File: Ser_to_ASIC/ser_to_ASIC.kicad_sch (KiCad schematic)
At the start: 44 parts, among them J1 MOLEX-524653071, J2 CONMHF4-SMD-G-T, J4 MOLEX-524653071, U1 ADP160AUJZ-1.2-R7, U2 ADP121-AUJZ12R7, U3 10M02DCV36I7G, U4 DS90UB913ATRTVJQ1, U5 TC2015-1.8VCTTR, U6 LT1761ES5-3.3-TRPBF, X1 EG-2102CA 100.0000M-PHPAL3

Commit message: Update ser_to_ASIC.kicad_sch
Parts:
- added C18: 10uF, symbol Device:C
- added R1, R10, R11: 10k, Resistor_SMD:R_0201_0603Metric, symbol Device:R_US
- added R2: 100k, Resistor_SMD:R_0201_0603Metric, symbol Device:R_US
- added SW1: R-668049, jonnew:MITSUMI_R-668049, symbol Switch:SW_Push
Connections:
- net +1V8: now also R1.2
- net +3.3V: now also R10.1, R11.1
- net G: now also U4.7 (RES), C18.2, R10.2, R2.1, SW1.1
- net SCL_SER: no longer R8.1, U4.4 (SCL)
- net SDA_SER: no longer R7.1, U4.5 (SDA)
- net at U4.8 (MODE): now also R1.1, R2.2
- net at U4.9 (PDB): now also C18.1, R11.2, SW1.2
- net ID_X: no longer names the net of R5.1, R6.1, U4.6 (ID[X])
- new net: R8.1, U4.4 (SCL)
- new net: R7.1, U4.5 (SDA)
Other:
- moved on the sheet: C1, C11, C12, C15, C16, C17, C2, C20, C21, C22, C23, C24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

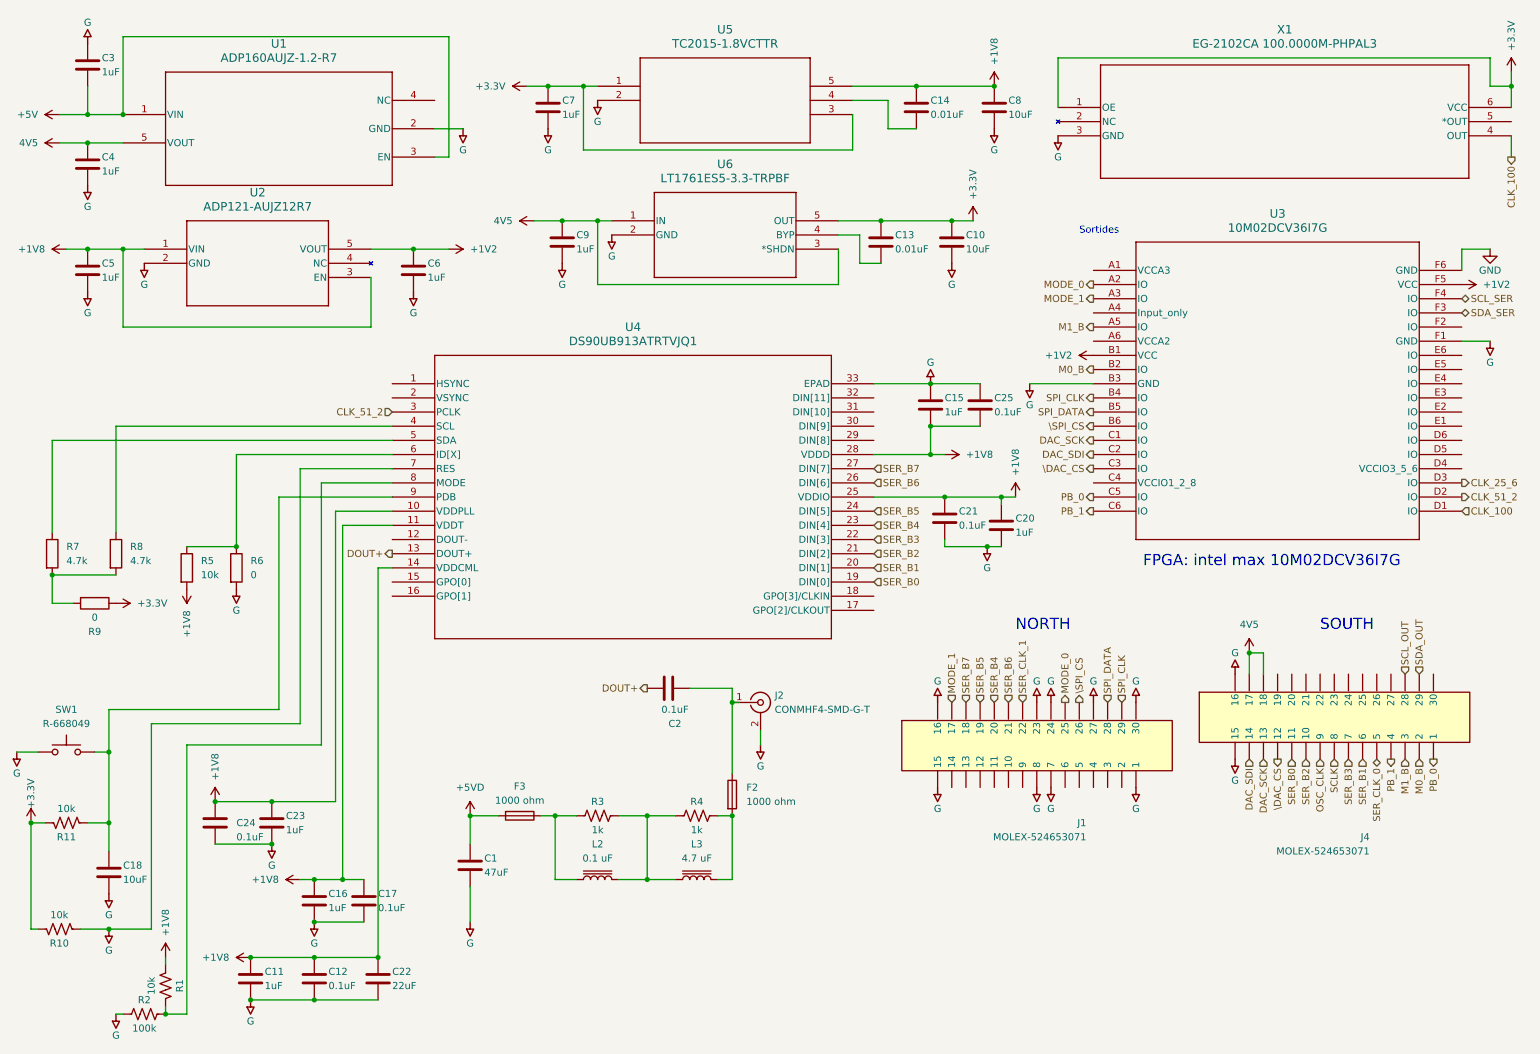
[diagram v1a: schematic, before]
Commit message: inici placa
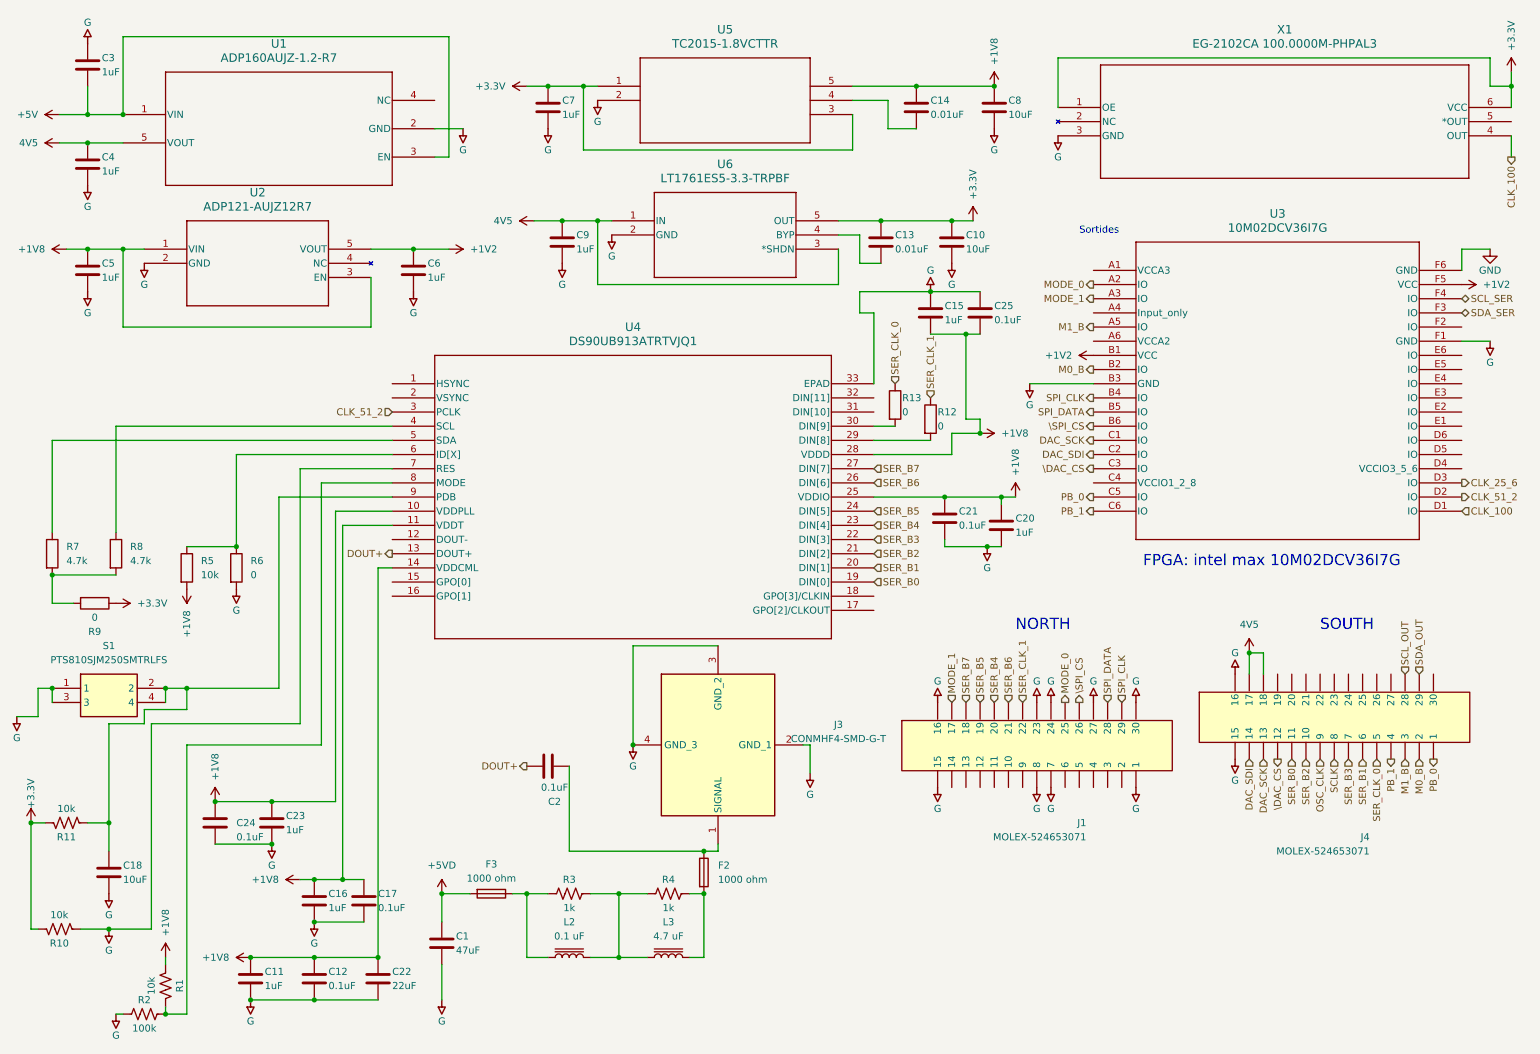
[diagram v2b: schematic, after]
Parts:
- removed J2: CONMHF4-SMD-G-T, Headstage-64s:Coax-Adapter, symbol Connector:Conn_Coaxial
- removed SW1: R-668049, jonnew:MITSUMI_R-668049, symbol Switch:SW_Push
- added J3: CONMHF4-SMD-G-T, llibreria_ser:CONMHF4SMDGT, symbol CONMHF4-SMD-G-T:CONMHF4-SMD-G-T
- added R12, R13: 0, Resistor_SMD:R_0402_1005Metric_Pad0.72x0.64mm_HandSolder, symbol Device:R
- added S1: PTS810SJM250SMTRLFS, PTS810SJG250SMTRLFS, symbol PTS810SJM250SMTRLFS:PTS810SJM250SMTRLFS
- C1: footprint Capacitor_SMD:C_0805_2012Metric -> Capacitor_SMD:C_1210_3225Metric
- C10, C13, C14, C3, C4, C5, C6, C7, C8, C9: footprint Capacitor_SMD:C_0201_0603Metric -> Capacitor_SMD:C_0805_2012Metric
- C11, C12, C15, C16, C17, C18, C20, C21, C23, C24, C25: footprint (none) -> Capacitor_SMD:C_0805_2012Metric
- C22: footprint (none) -> Capacitor_SMD:C_1210_3225Metric
- F2, F3: footprint (none) -> Fuse:Fuse_0805_2012Metric
- J1, J4: footprint FDM_footprints:J524653071_Board2Board -> llibreria_ser:J524653071
- L2, L3: footprint (none) -> Inductor_SMD:L_1210_3225Metric
- R1, R10, R11, R2, R3, R4: footprint Resistor_SMD:R_0201_0603Metric -> Resistor_SMD:R_0402_1005Metric_Pad0.72x0.64mm_HandSolder
- U3: footprint VBGA/WLCSP36_A0p54_INT -> llibreria_ser:VBGA&slash_WLCSP36_A0p54_INT
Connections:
- net G: now also J3.2 (GND_1), J3.3 (GND_2), J3.4 (GND_3), S1.1, S1.3
- net SER_CLK_0: now also R13.1
- net SER_CLK_1: now also R12.1
- net at C18.1, R11.2, U4.9 (PDB): now also S1.2, S1.4
- net at C2.1, F2.1: now also J3.1 (SIGNAL)
- net at U4.29 (DIN[8]): now also R12.2
- net at U4.30 (DIN[9]): now also R13.2
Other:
- moved on the sheet: C1, C15, C2, C25, F2, F3, L2, L3, R3, R4

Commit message: actualitzacio
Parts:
- C10, C11, C12, C13, C14, C15, C16, C17, C18, C2, C20, C21, C23, C24, C25, C3, C4, C5, C6, C7, C8, C9: footprint Capacitor_SMD:C_0805_2012Metric -> Capacitor_SMD:C_0603_1608Metric
- R1, R10, R11, R12, R13, R2, R3, R4, R5, R6, R7, R8, R9: footprint Resistor_SMD:R_0402_1005Metric_Pad0.72x0.64mm_HandSolder -> Resistor_SMD:R_0603_1608Metric
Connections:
- net GND is gone; now on net G: U3.F6 (GND)
- net +3.3V: now also U3.A1 (VCCA3), U3.A6 (VCCA2), U3.C4 (VCCIO1_2_8), U3.D4 (VCCIO3_5_6)
- net CLK_100: now also U3.A3 (IO); no longer U3.D1 (IO)
- net CLK_25_6: now also U3.E1 (IO); no longer U3.D3 (IO)
- net DAC_SCK: now also U3.B6 (IO); no longer U3.C1 (IO)
- net DAC_SDI: now also U3.B4 (IO); no longer U3.C2 (IO)
- net M0_B: now also U3.D6 (IO); no longer U3.B2 (IO)
- net M1_B: now also U3.F4 (IO); no longer U3.A5 (IO)
- net MODE_1: now also U3.C2 (IO); no longer U3.A3 (IO)
- net PB_0: now also U3.E6 (IO); no longer U3.C5 (IO)
- net PB_1: now also U3.C5 (IO); no longer U3.C6 (IO)
- net SCL_SER: now also R8.1, U3.B5 (IO), U4.4 (SCL); no longer U3.F4 (IO)
- net SDA_SER: now also R7.1, U3.A5 (IO), U4.5 (SDA); no longer U3.F3 (IO)
- net SPI_CLK: now also U3.D1 (IO); no longer U3.B4 (IO)
- net SPI_DATA: now also U3.C1 (IO); no longer U3.B5 (IO)
- net \DAC_CS: now also U3.C6 (IO); no longer U3.C3 (IO)
- net \SPI_CS: now also U3.F3 (IO); no longer U3.B6 (IO)

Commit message: ACTUALITZACIO
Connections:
- net CLK_25_6 is gone; now on net OSC_CLK: U3.E1 (IO)
- net CLK_51_2 is gone; now on net SCLK: U3.D2 (IO), U4.3 (PCLK)
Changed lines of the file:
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@@
     (effects (font (size 1.27 1.27)) (justify left))
   )
-  (hierarchical_label "CLK_51_2" (shape input) (at 81.28 83.82 180) (fields_autoplaced)
+  (hierarchical_label "SCLK" (shape input) (at 81.28 83.82 180) (fields_autoplaced)
     (effects (font (size 1.27 1.27)) (justify right))
   )
@@
     (effects (font (size 1.27 1.27)) (justify left))
   )
-  (hierarchical_label "CLK_25_6" (shape output) (at 273.05 86.36 0) (fields_autoplaced)
+  (hierarchical_label "OSC_CLK" (shape output) (at 273.05 86.36 0) (fields_autoplaced)
     (effects (font (size 1.27 1.27)) (justify left))
   )
@@
     (effects (font (size 1.27 1.27)) (justify right))
   )
-  (hierarchical_label "CLK_51_2" (shape output) (at 273.05 99.06 0) (fields_autoplaced)
+  (hierarchical_label "SCLK" (shape output) (at 273.05 99.06 0) (fields_autoplaced)
     (effects (font (size 1.27 1.27)) (justify left))
   )
